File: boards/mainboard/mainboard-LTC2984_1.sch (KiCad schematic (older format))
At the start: 33 parts, among them U401 LTC2984

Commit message: [mainboard] layout: footprints assigned, first placement
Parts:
- R402: footprint Resistors_ThroughHole:Resistor_Horizontal_RM7mm -> Resistors_THT:R_Axial_DIN0204_L3.6mm_D1.6mm_P5.08mm_Horizontal
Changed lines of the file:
@@
 F 0 "R402" V 4350 2200 50  0000 C CNN
 F 1 "2k00" V 4450 2200 50  0000 C CNN
-F 2 "Resistors_ThroughHole:Resistor_Horizontal_RM7mm" V 4380 2200 50  0001 C CNN
+F 2 "Resistors_THT:R_Axial_DIN0204_L3.6mm_D1.6mm_P5.08mm_Horizontal" V 4380 2200 50  0001 C CNN
 F 3 "" H 4450 2200 50  0000 C CNN
 	1    4450 2200
@@
 $EndComp
 $Comp
-L GND #PWR030
+L GND #PWR028
 U 1 1 587B0B78
 P 5650 1600
-F 0 "#PWR030" H 5650 1350 50  0001 C CNN
+F 0 "#PWR028" H 5650 1350 50  0001 C CNN
 F 1 "GND" H 5650 1450 50  0000 C CNN
 F 2 "" H 5650 1600 50  0000 C CNN
@@
 $EndComp
 $Comp
-L GND #PWR031
+L GND #PWR029
 U 1 1 58FFF57E
 P 5650 4850
-F 0 "#PWR031" H 5650 4600 50  0001 C CNN
+F 0 "#PWR029" H 5650 4600 50  0001 C CNN
 F 1 "GND" H 5650 4700 50  0000 C CNN
 F 2 "" H 5650 4850 50  0000 C CNN
@@
 $EndComp
 $Comp
-L GND #PWR032
+L GND #PWR030
 U 1 1 587B5000
 P 8200 1750
-F 0 "#PWR032" H 8200 1500 50  0001 C CNN
+F 0 "#PWR030" H 8200 1500 50  0001 C CNN
 F 1 "GND" H 8200 1600 50  0000 C CNN
 F 2 "" H 8200 1750 50  0000 C CNN
@@
 $EndComp
 $Comp
-L GND #PWR033
+L GND #PWR031
 U 1 1 58FFF590
 P 7000 1150
-F 0 "#PWR033" H 7000 900 50  0001 C CNN
+F 0 "#PWR031" H 7000 900 50  0001 C CNN
 F 1 "GND" H 7000 1000 50  0000 C CNN
 F 2 "" H 7000 1150 50  0000 C CNN
@@
 $EndComp
 $Comp
-L GND #PWR034
+L GND #PWR032
 U 1 1 587B5F5F
 P 7100 5050
-F 0 "#PWR034" H 7100 4800 50  0001 C CNN
+F 0 "#PWR032" H 7100 4800 50  0001 C CNN
 F 1 "GND" H 7100 4900 50  0000 C CNN
 F 2 "" H 7100 5050 50  0000 C CNN
@@
 $EndComp
 $Comp
-L GND #PWR035
+L GND #PWR033
 U 1 1 58FFF5AE
 P 7300 6150
-F 0 "#PWR035" H 7300 5900 50  0001 C CNN
+F 0 "#PWR033" H 7300 5900 50  0001 C CNN
 F 1 "GND" H 7300 6000 50  0000 C CNN
 F 2 "" H 7300 6150 50  0000 C CNN
@@
 $EndComp
 $Comp
-L GND #PWR036
+L GND #PWR034
 U 1 1 58FFF5B6
 P 7250 1250
-F 0 "#PWR036" H 7250 1000 50  0001 C CNN
+F 0 "#PWR034" H 7250 1000 50  0001 C CNN
 F 1 "GND" H 7250 1100 50  0000 C CNN
 F 2 "" H 7250 1250 50  0000 C CNN
@@
 $EndComp
 $Comp
-L GND #PWR037
+L GND #PWR035
 U 1 1 587BD508
 P 7650 1050
-F 0 "#PWR037" H 7650 800 50  0001 C CNN
+F 0 "#PWR035" H 7650 800 50  0001 C CNN
 F 1 "GND" H 7650 900 50  0000 C CNN
 F 2 "" H 7650 1050 50  0000 C CNN
@@
 $EndComp
 $Comp
-L GND #PWR038
+L GND #PWR036
 U 1 1 58FFF5C6
 P 6550 4600
-F 0 "#PWR038" H 6550 4350 50  0001 C CNN
+F 0 "#PWR036" H 6550 4350 50  0001 C CNN
 F 1 "GND" H 6550 4450 50  0000 C CNN
 F 2 "" H 6550 4600 50  0000 C CNN
@@
 VREF_BYP
 $Comp
-L +3V3 #PWR039
+L +3V3 #PWR037
 U 1 1 58FFF5CA
 P 7500 5050
-F 0 "#PWR039" H 7500 4900 50  0001 C CNN
+F 0 "#PWR037" H 7500 4900 50  0001 C CNN
 F 1 "+3V3" H 7500 5190 50  0000 C CNN
 F 2 "" H 7500 5050 50  0000 C CNN
@@
 $EndComp
 $Comp
-L +3V3 #PWR040
+L +3V3 #PWR038
 U 1 1 58FFF5D1
 P 7300 5450
-F 0 "#PWR040" H 7300 5300 50  0001 C CNN
+F 0 "#PWR038" H 7300 5300 50  0001 C CNN
 F 1 "+3V3" H 7300 5590 50  0000 C CNN
 F 2 "" H 7300 5450 50  0000 C CNN
@@
 	4300 2000 4250 2000
 $Comp
-L +3V3 #PWR041
+L +3V3 #PWR039
 U 1 1 587EB89F
 P 9050 3400
-F 0 "#PWR041" H 9050 3250 50  0001 C CNN
+F 0 "#PWR039" H 9050 3250 50  0001 C CNN
 F 1 "+3V3" H 9050 3540 50  0000 C CNN
 F 2 "" H 9050 3400 50  0000 C CNN
@@
 $EndComp
 $Comp
-L +3V3 #PWR042
+L +3V3 #PWR040
 U 1 1 58FFF5EF
 P 8550 1900
-F 0 "#PWR042" H 8550 1750 50  0001 C CNN
+F 0 "#PWR040" H 8550 1750 50  0001 C CNN
 F 1 "+3V3" H 8550 2040 50  0000 C CNN
 F 2 "" H 8550 1900 50  0000 C CNN

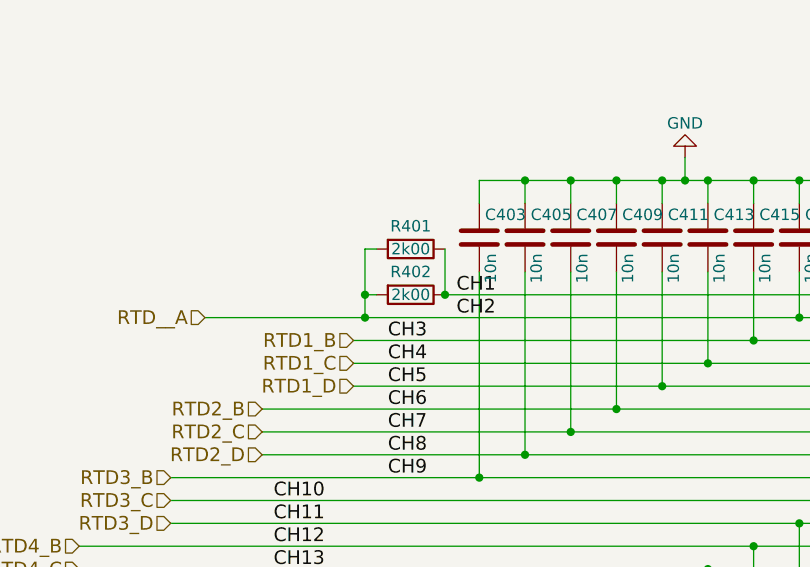
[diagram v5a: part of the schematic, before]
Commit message: [mainboard] first traces routed, some pins in schematic swapped
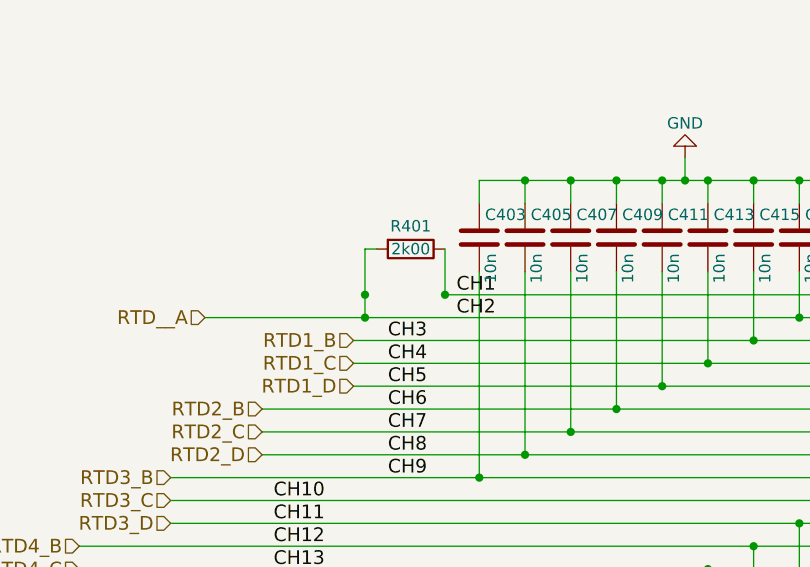
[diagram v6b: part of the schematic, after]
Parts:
- removed R402: 2k00, Resistors_THT:R_Axial_DIN0204_L3.6mm_D1.6mm_P5.08mm_Horizontal, symbol R
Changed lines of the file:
@@
-$EndComp
-$Comp
-L R R402
-U 1 1 58FFF511
-P 4450 2200
-F 0 "R402" V 4350 2200 50  0000 C CNN
-F 1 "2k00" V 4450 2200 50  0000 C CNN
-F 2 "Resistors_THT:R_Axial_DIN0204_L3.6mm_D1.6mm_P5.08mm_Horizontal" V 4380 2200 50  0001 C CNN
-F 3 "" H 4450 2200 50  0000 C CNN
-	1    4450 2200
-	0    1    1    0
 $EndComp
 $Comp
@@
 Wire Wire Line
 	9050 3400 8950 3400
-Wire Wire Line
-	4250 2200 4300 2200
 Text HLabel 4200 2400 0    60   Input ~ 0
 RTD1_B
